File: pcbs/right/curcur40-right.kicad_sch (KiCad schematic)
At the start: 80 parts

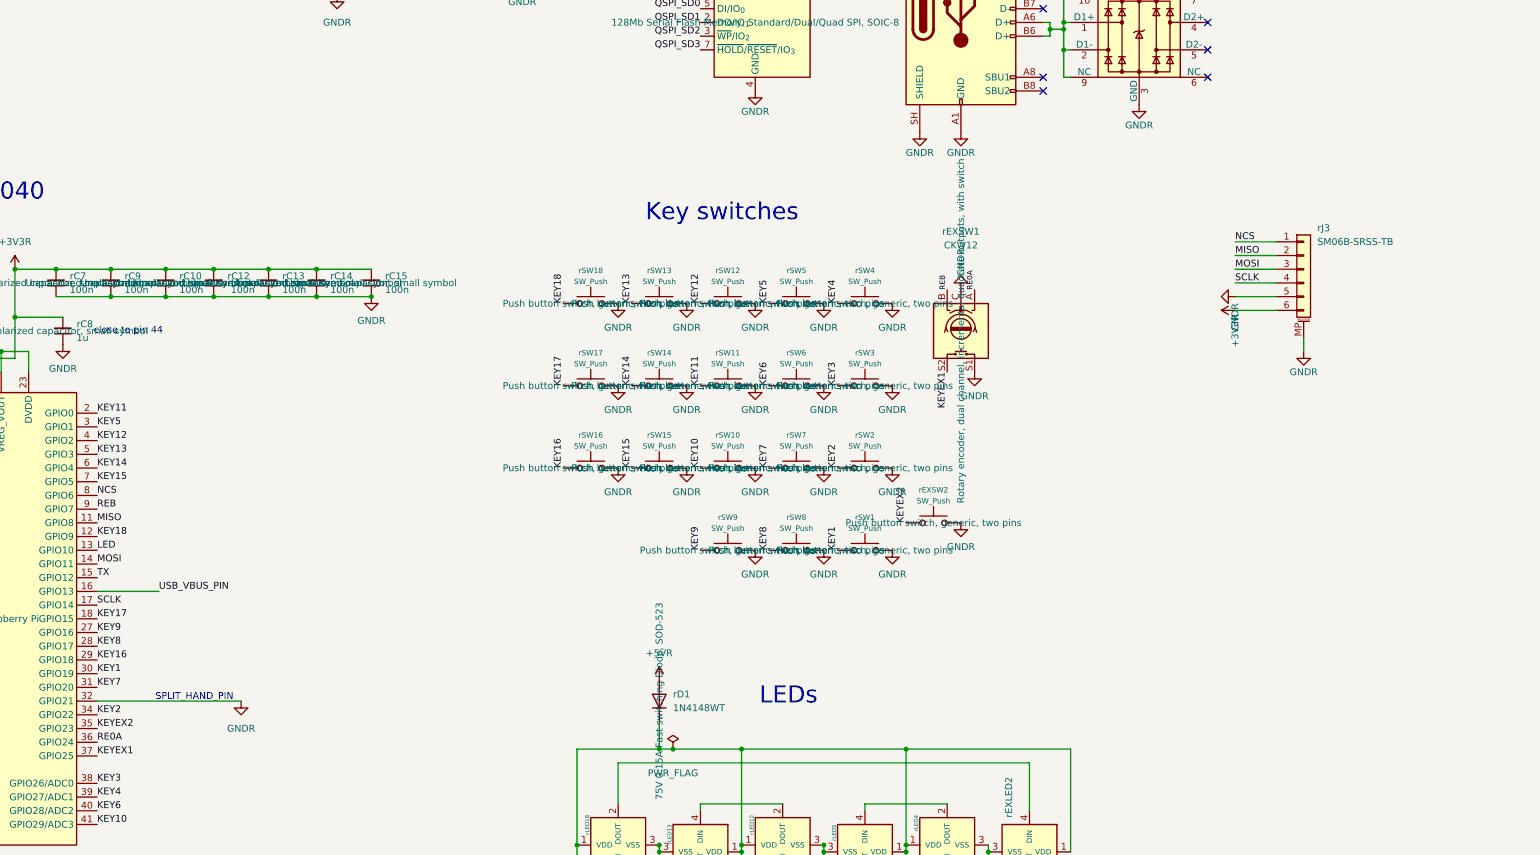
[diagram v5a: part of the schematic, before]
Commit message: feat(pcb): integrate sunk inertia wheel cutout and rJ5 connector into curcur40-right and top plate
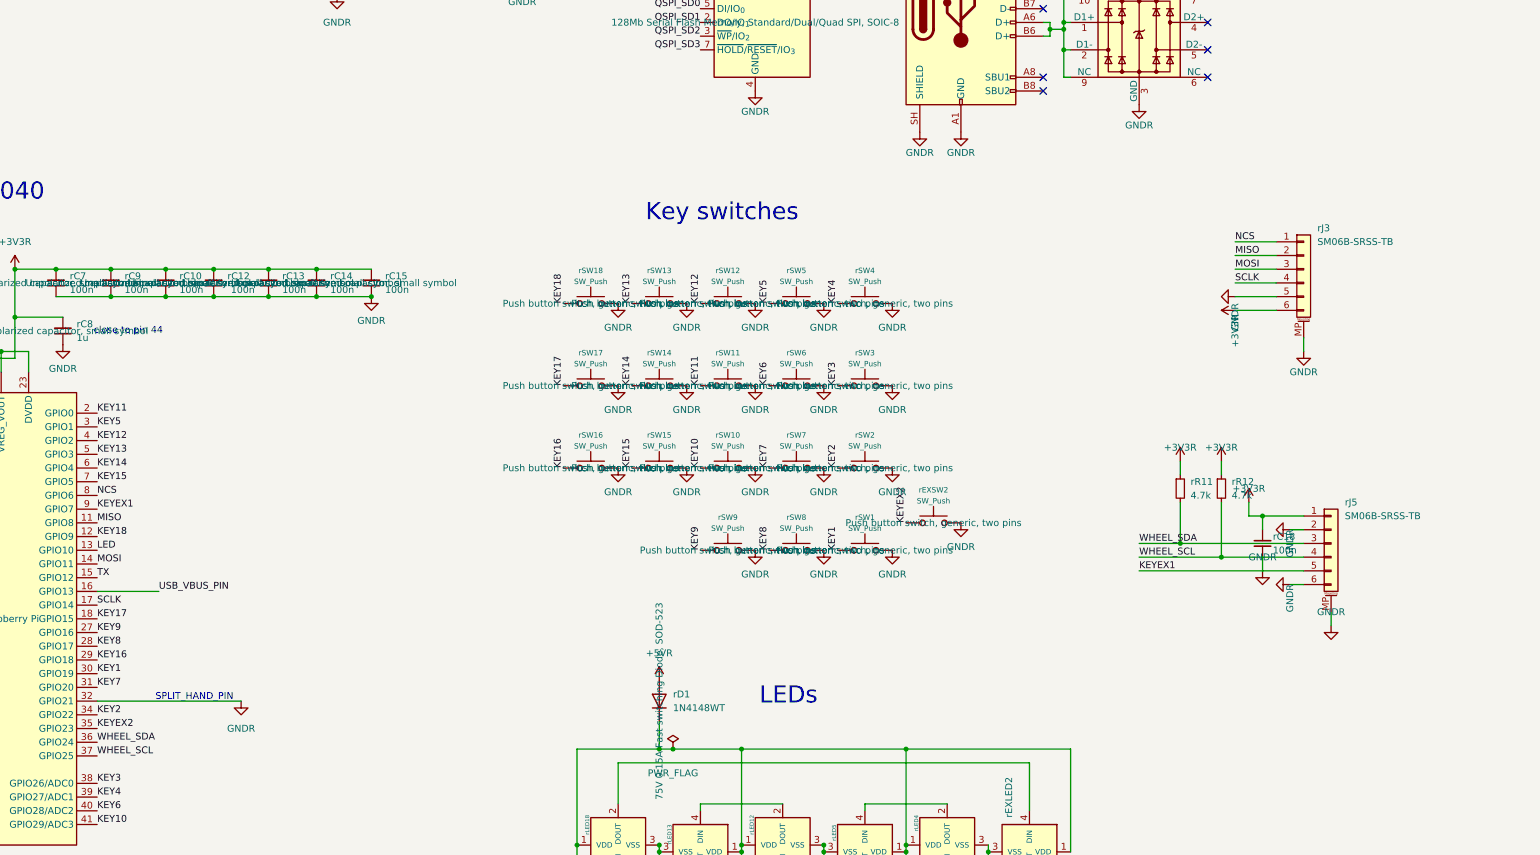
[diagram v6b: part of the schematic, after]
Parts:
- removed rEXSW1: CKW12, kbd:RotaryEncoder_Switch_CKW12, symbol Device:RotaryEncoder_Switch
- added rC18: 100n, Capacitor_SMD:C_0402_1005Metric, symbol Device:C_Small
- added rJ5: SM06B-SRSS-TB, Connector_JST:JST_SH_SM06B-SRSS-TB_1x06-1MP_P1.00mm_Horizontal, symbol Connector_Generic_MountingPin:Conn_01x06_MountingPin
- added rR11, rR12: 4.7k, Resistor_SMD:R_0402_1005Metric, symbol Device:R_Small
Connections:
- net REB is gone; now on net KEYEX1: rU1.9 (GPIO7)
- net +3V3R: now also rC18.1, rJ5.1 (Pin_1), rR11.1, rR12.1
- net GNDR: now also rC18.2, rJ5.2 (Pin_2), rJ5.6 (Pin_6), rJ5.MP (MountPin)
- net KEYEX1: now also rJ5.5 (Pin_5); no longer rU1.37 (GPIO25)
- net RE0A renamed WHEEL_SDA
- net WHEEL_SDA: now also rJ5.3 (Pin_3), rR11.2
- new net WHEEL_SCL: rJ5.4 (Pin_4), rR12.2, rU1.37 (GPIO25)
